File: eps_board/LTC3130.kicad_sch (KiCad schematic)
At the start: 15 parts, among them U83 LTC3130-1

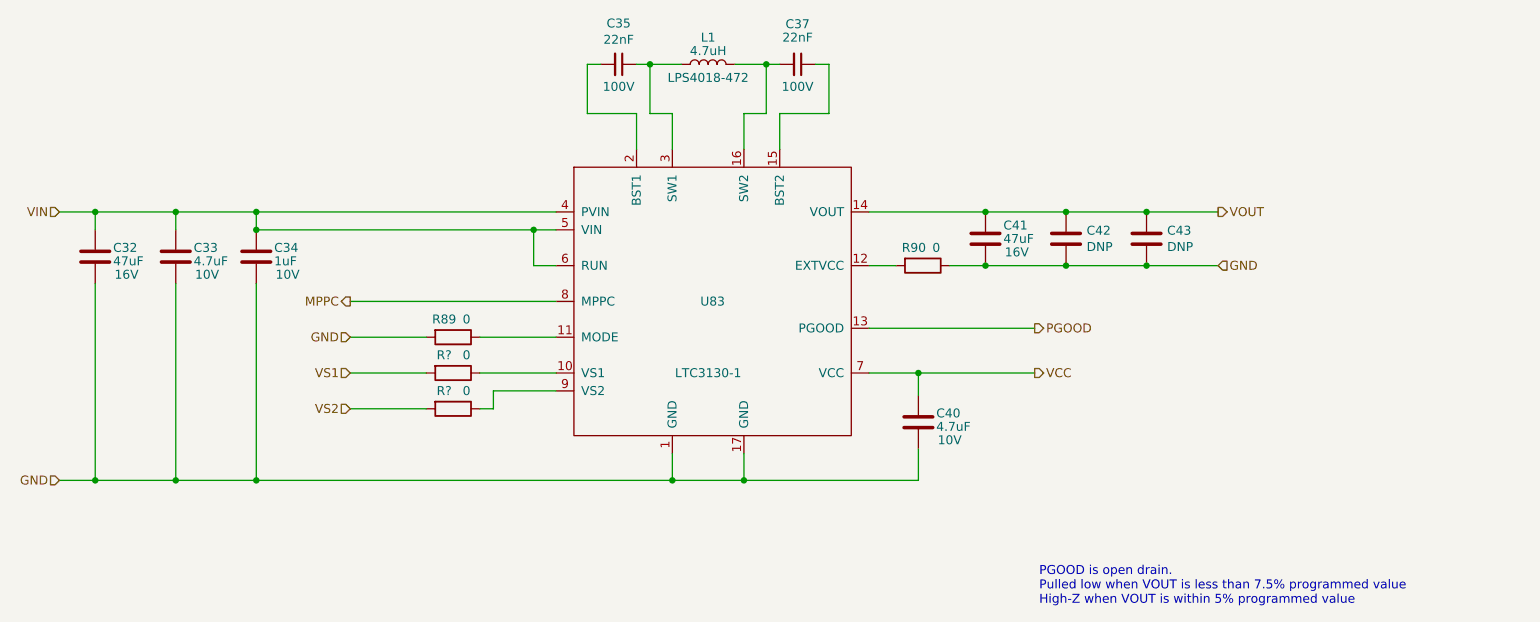
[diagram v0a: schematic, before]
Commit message: EPS: cleaning up, footprint to 80x80, and replace discrete switches with ICs for switch and measurement
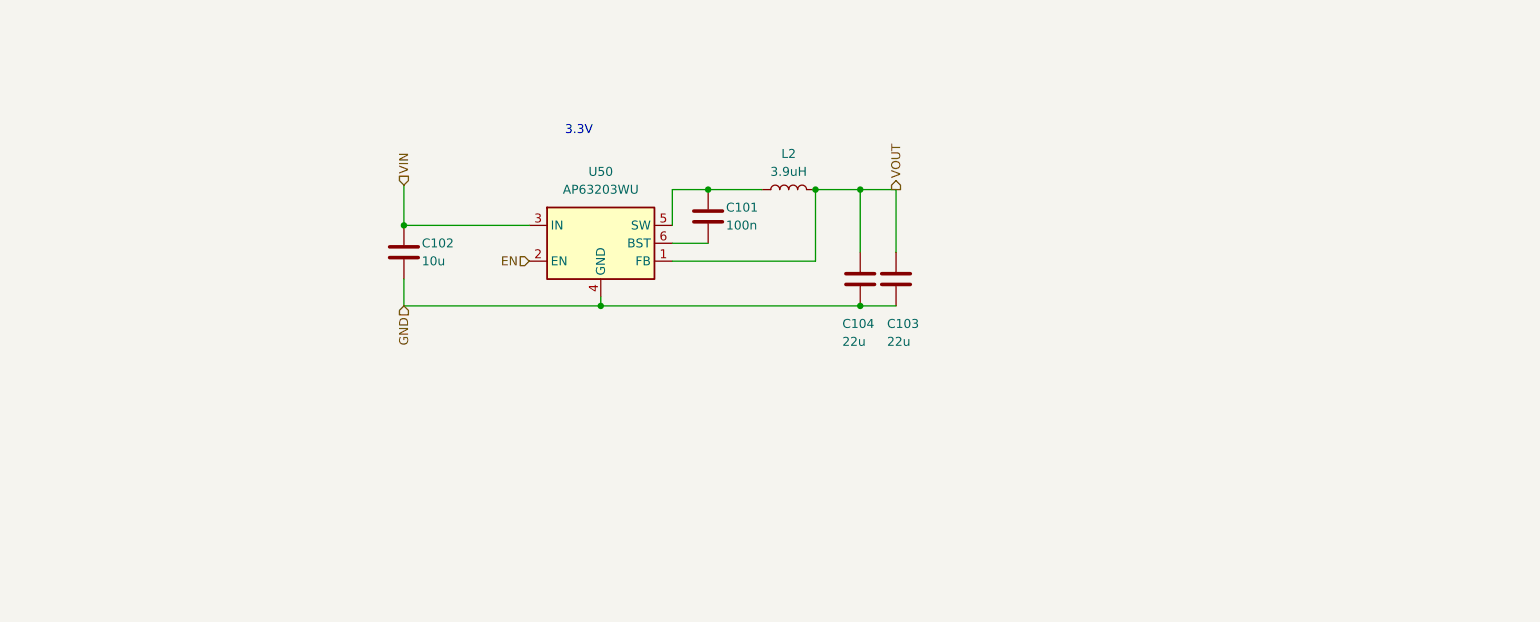
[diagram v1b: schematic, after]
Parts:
- removed C32, C41: 47uF, Capacitor_SMD:C_1210_3225Metric_Pad1.42x2.65mm_HandSolder, symbol Device:C
- removed C33, C40: 4.7uF, Capacitor_SMD:C_0603_1608Metric_Pad1.05x0.95mm_HandSolder, symbol Device:C
- removed C34: 1uF, Capacitor_SMD:C_0603_1608Metric_Pad1.05x0.95mm_HandSolder, symbol Device:C
- removed C35, C37: 22nF, Capacitor_SMD:C_0603_1608Metric_Pad1.05x0.95mm_HandSolder, symbol Device:C_Small
- removed C42: DNP, Capacitor_SMD:C_1210_3225Metric_Pad1.42x2.65mm_HandSolder, symbol Device:C
- removed C43: DNP, Capacitor_SMD:C_0603_1608Metric_Pad1.05x0.95mm_HandSolder, symbol Device:C
- removed L1: 4.7uH, Inductor_SMD:L_Coilcraft_LPS4018, symbol Device:L
- removed R89, R90, R? (x2): 0, Resistor_SMD:R_0603_1608Metric_Pad1.05x0.95mm_HandSolder, symbol Device:R
- removed U83: LTC3130-1, footprint_custom:MSOP-16-1EP_3x4.039mm_P0.5mm_EP1.651x2.845mm_0.3mmThermalVias, symbol EPS-rescue:LTC3130-1-1K_Custom_Symbol
- added C101: 100n, Capacitor_SMD:C_0402_1005Metric_Pad0.74x0.62mm_HandSolder, symbol Device:C
- added C102: 10u, Capacitor_SMD:C_0603_1608Metric_Pad1.08x0.95mm_HandSolder, symbol Device:C
- added C103, C104: 22u, Capacitor_SMD:C_0805_2012Metric_Pad1.18x1.45mm_HandSolder, symbol Device:C
- added L2: 3.9uH, Inductor_SMD:L_1210_3225Metric_Pad1.42x2.65mm_HandSolder, symbol Device:L
- added U50: AP63203WU, Package_TO_SOT_SMD:TSOT-23-6_HandSoldering, symbol Regulator_Switching:AP63203WU
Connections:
- net GND: now also C102.2, C103.2, C104.2, U50.4 (GND)
- net VIN: now also C102.1, U50.3 (IN)
- net VOUT: now also C103.1, C104.1, L2.2, U50.1 (FB)
- new net: C101.1, L2.1, U50.5 (SW)
- new net: C101.2, U50.6 (BST)
- new net EN: U50.2 (EN)
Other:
- note added: "3.3V"
- note removed: "PGOOD is open drain. Pulled low when VOUT is less than 7.5% programmed value High-Z when VOUT is within 5% programmed value"

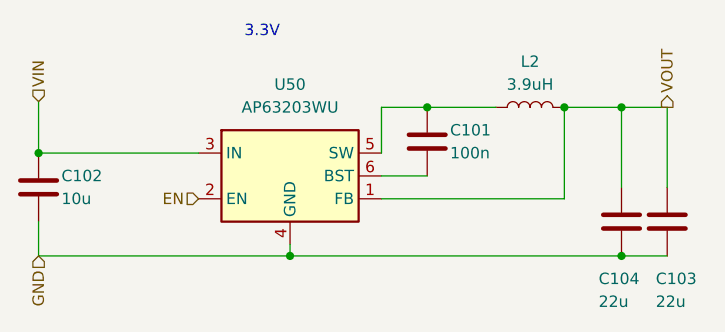
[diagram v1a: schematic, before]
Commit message: combine interrupts per powerline and use i2c expanders to turn on and solicit feedback
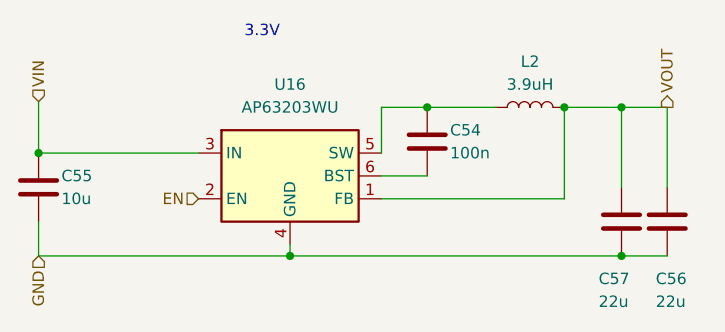
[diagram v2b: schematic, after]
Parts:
- renumbered C101 to C54, C102 to C55, C103 to C56, C104 to C57, U50 to U16
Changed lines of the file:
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@@
 		(dnp no)
 		(fields_autoplaced yes)
-		(property "Reference" "U50"
+		(property "Reference" "U16"
 			(at 118.11 78.74 0)
 			(effects
@@
 			(project "EPS"
 				(path "/05170af6-30ef-4c3a-b972-f098085da1bc/00000000-0000-0000-0000-00005fcd393e"
-					(reference "U50")
+					(reference "U16")
 					(unit 1)
 				)
@@
 		(on_board yes)
 		(dnp no)
-		(property "Reference" "C102"
+		(property "Reference" "C55"
 			(at 92.71 88.9 0)
 			(effects
@@
 			(project "EPS"
 				(path "/05170af6-30ef-4c3a-b972-f098085da1bc/00000000-0000-0000-0000-00005fcd393e"
-					(reference "C102")
+					(reference "C55")
 					(unit 1)
 				)
@@
 		(on_board yes)
 		(dnp no)
-		(property "Reference" "C101"
+		(property "Reference" "C54"
 			(at 135.89 83.82 0)
 			(effects
@@
 			(project "EPS"
 				(path "/05170af6-30ef-4c3a-b972-f098085da1bc/00000000-0000-0000-0000-00005fcd393e"
-					(reference "C101")
+					(reference "C54")
 					(unit 1)
 				)
@@
 		(on_board yes)
 		(dnp no)
-		(property "Reference" "C103"
+		(property "Reference" "C56"
 			(at 158.75 100.33 0)
 			(effects
@@
 			(project "EPS"
 				(path "/05170af6-30ef-4c3a-b972-f098085da1bc/00000000-0000-0000-0000-00005fcd393e"
-					(reference "C103")
+					(reference "C56")
 					(unit 1)
 				)
@@
 		(on_board yes)
 		(dnp no)
-		(property "Reference" "C104"
+		(property "Reference" "C57"
 			(at 152.4 100.33 0)
 			(effects
@@
 			(project "EPS"
 				(path "/05170af6-30ef-4c3a-b972-f098085da1bc/00000000-0000-0000-0000-00005fcd393e"
-					(reference "C104")
+					(reference "C57")
 					(unit 1)
 				)
